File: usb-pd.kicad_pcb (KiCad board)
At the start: 2 copper layers, 45 x 20 mm, 15 parts, among them J1 USB_C_Receptacle_PowerOnly_6P, J2 USB3_A, Q1 AO3401A, U1 CYPD3177-24LQ, U2 AMS1117-3.3

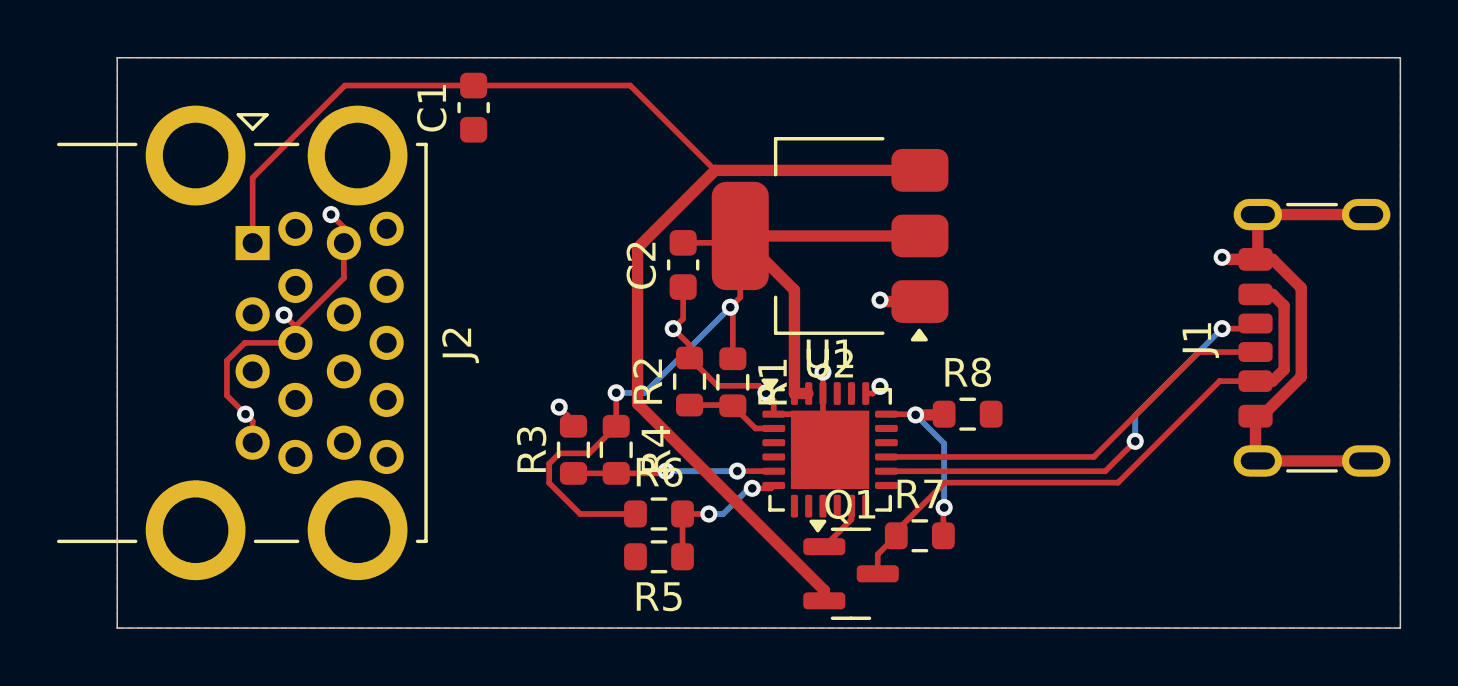
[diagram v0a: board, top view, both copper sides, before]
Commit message: adding silkscreen and stuff
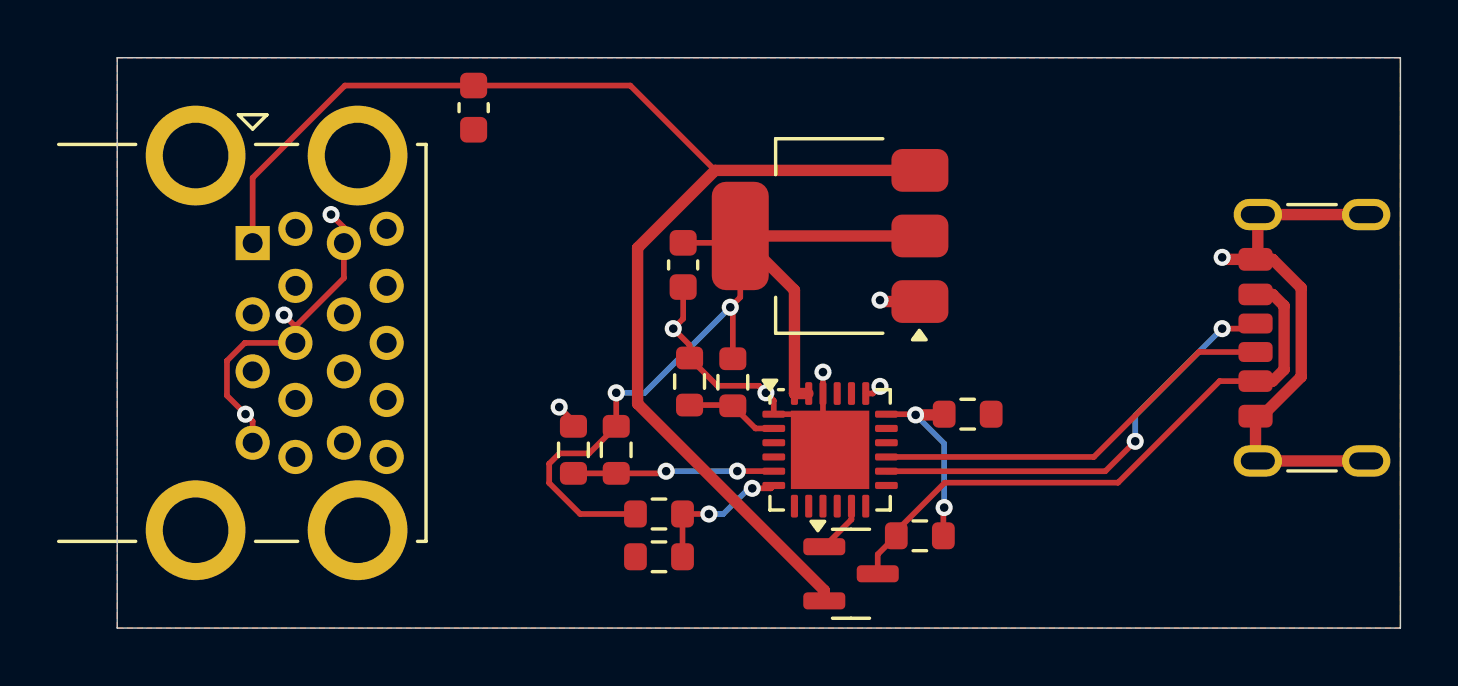
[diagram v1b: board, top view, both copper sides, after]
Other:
- board text added: "USB-C PD Charger up to 12V/3A"
